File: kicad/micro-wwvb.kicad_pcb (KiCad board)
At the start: 2 copper layers, 42.5 x 40.6 mm, 20 parts, among them J2 USB_B_Mini, U1 ATtiny44A, Y1 Crystal

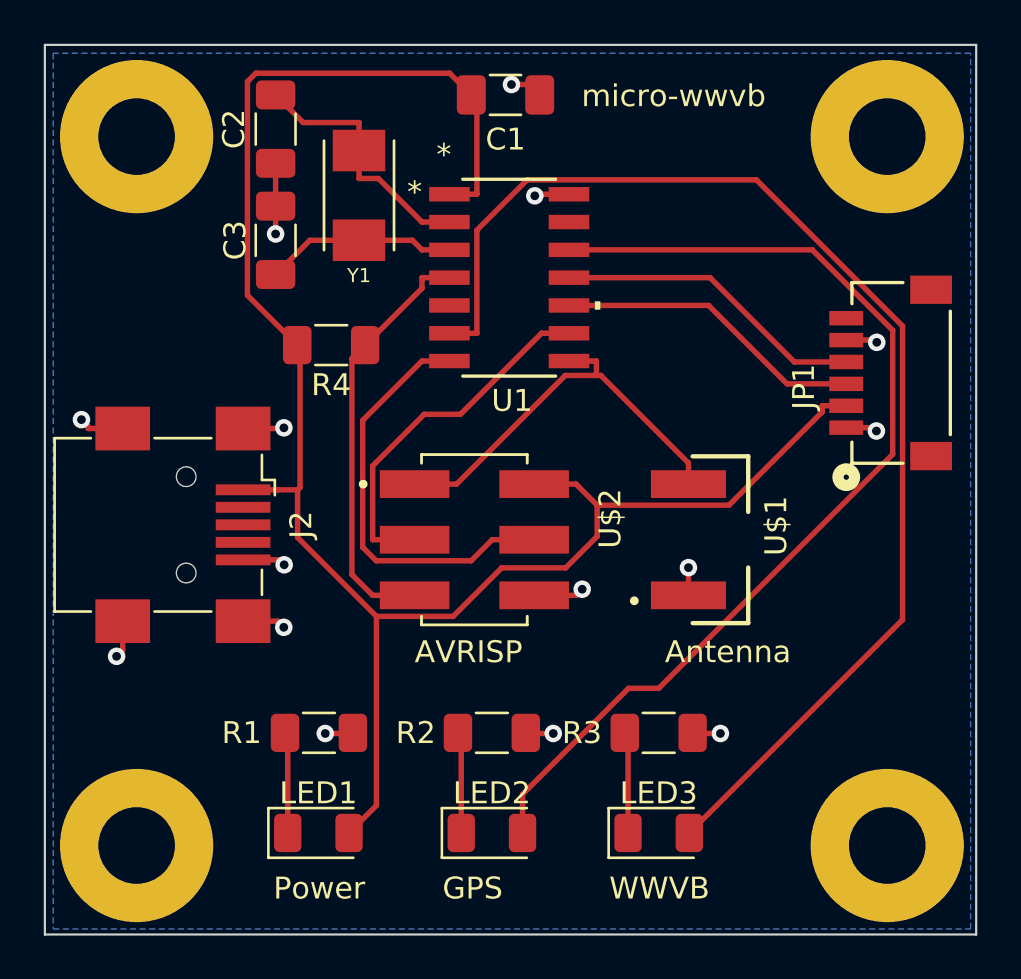
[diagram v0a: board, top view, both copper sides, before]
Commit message: Yikes!  I reversed all the pins on the gps connector.
I didn't realize the plug had to be turned
upside down to fit it into the connector.

The kicad files have been updated.  It also seems
I've swapped the transmit and receive on the gps
connector.  I've updated the code to compensate.
Found compatibility problems when using a windows
version of make.  Updated the makefile.
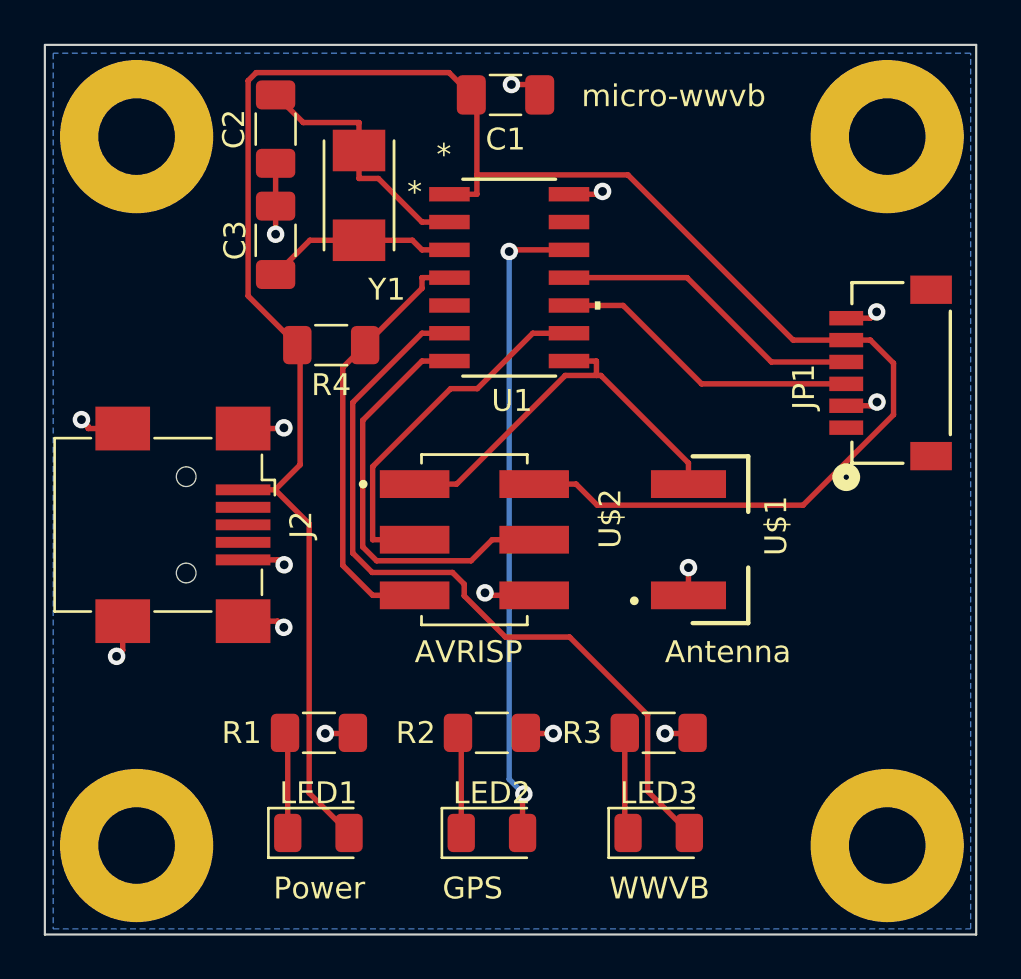
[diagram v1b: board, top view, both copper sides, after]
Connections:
- JP1 pad 1: GND -> unconnected-(JP1-Pad1)
- JP1 pad 2: VCC -> GND
- JP1 pad 5: GND -> VCC
- JP1 pad 6: unconnected-(JP1-Pad6) -> GND
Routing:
- net Net-(LED3-A): track 56.3 -> 35.6 mm
- net Net-(LED2-A): track 47.1 -> 29.6 mm, vias 0 -> 2
- net VCC: track 86.3 -> 98.8 mm
